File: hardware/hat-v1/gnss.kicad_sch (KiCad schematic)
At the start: 10 parts, among them J4 U.FL, U14 MAX-M10S-00B

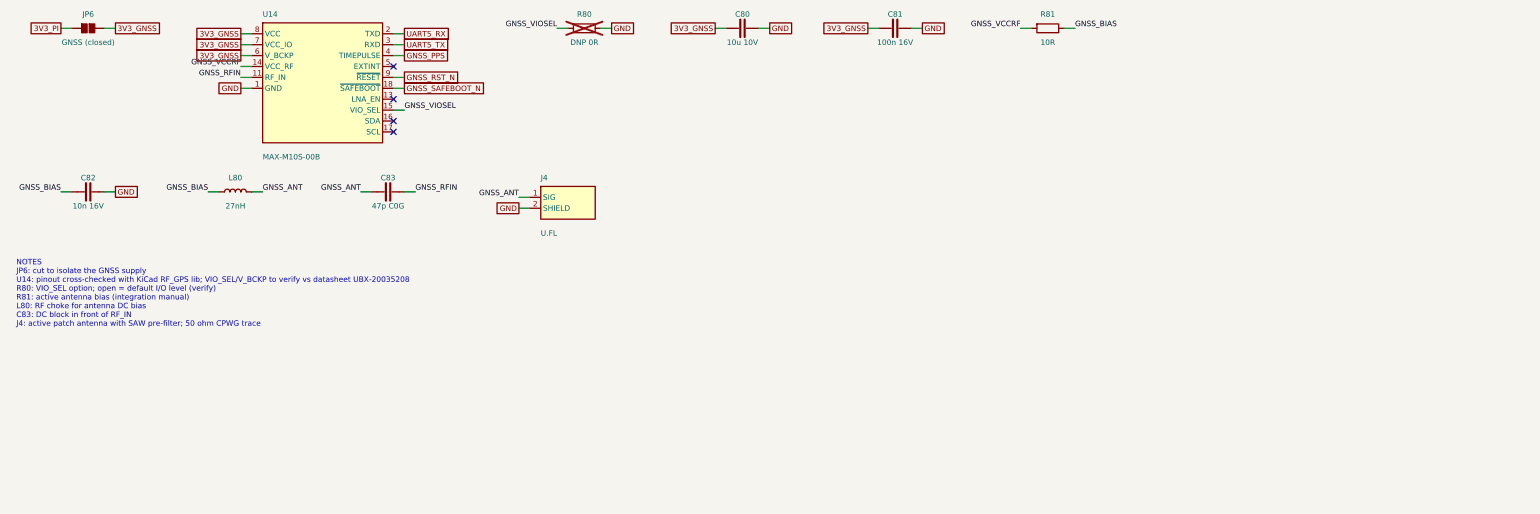
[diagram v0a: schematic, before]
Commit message: HAT v1 schematic: apply adversarial review (power + digital/security/DFM)
AUTO-ON above buck EN window, BENCH no longer blocks power-off, OVP moved
to 19.2 V with input damper, Tier A parts DNP for JLC, debug links
removable for production, antenna short limited, stock footprints where
available, cap ratings/DC-bias fixes, CONSOLE_TX/RX naming.

Co-Authored-By: Claude Opus 5.5 <noreply@anthropic.com>
Claude-Session: https://claude.ai/code/session_01MLRuxTEmuMV82xcNLE62jW
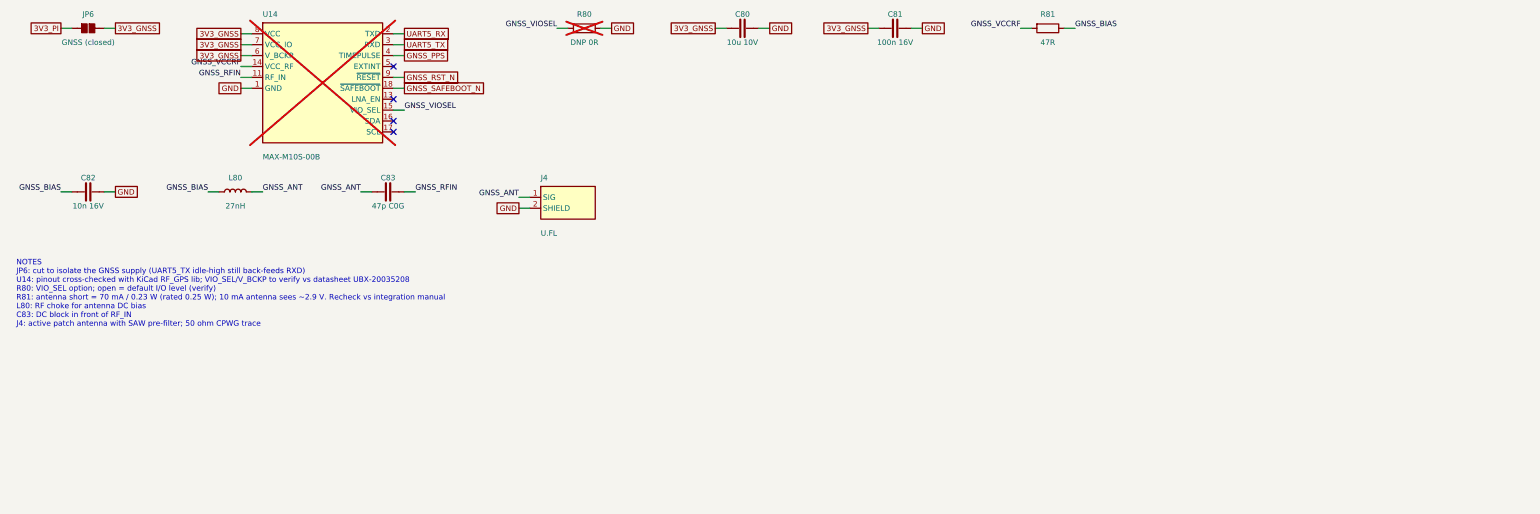
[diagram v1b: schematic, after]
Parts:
- JP6: Note cut to isolate the GNSS supply -> cut to isolate the GNSS supply (UART5_TX idle-high still ba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; now left out of the parts list
- R81: value 10R -> 47R; footprint Resistor_SMD:R_0402_1005Metric -> Resistor_SMD:R_1206_3216Metric; Note active antenna bias (integration manual) -> antenna short = 70 mA / 0.23 W (rated 0.25 W); 10 mA antenn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
- U14: now not fitted
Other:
- note added: "NOTES JP6: cut to isolate the GNSS supply (UART5_TX idle-high still back-feeds RXD) U14: pinout cross-checked with KiCad RF_GPS lib; VIO_SEL/V_BCKP to verify vs datasheet UBX-20035208 R80: VIO_SEL option; open = default I/O level (verify) R81: antenna short = 70 mA / 0.23 W (rated 0.25 W); 10 mA antenna sees ~2.9 V. Recheck vs integration manual L80: RF choke for antenna DC bias C83: DC block in 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"
- note removed: "NOTES JP6: cut to isolate the GNSS supply U14: pinout cross-checked with KiCad RF_GPS lib; VIO_SEL/V_BCKP to verify vs datasheet UBX-20035208 R80: VIO_SEL option; open = default I/O level (verify) R81: active antenna bias (integration manual) L80: RF choke for antenna DC bias C83: DC block in front of RF_IN J4: active patch antenna with SAW pre-filter; 50 ohm CPWG trace"
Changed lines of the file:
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@@
   (paper "A4")
   (title_block (title "Batman HAT v1 (Pi 4) - replaces Seeed WM1302 HAT") (date "2026-09-27") (rev "0.1-draft") (company "Batman project - generated by hardware/hat-v1/gen/gen_sch.py, do not edit by hand") (comment 1 "8 GNSS MAX-M10S + active antenna bias") (comment 2 "Label-based schematic: same net name = connected"))
-  (symbol (lib_id "batman:SJ") (at 31.75 26.67 0) (unit 1) (in_bom yes) (on_board yes) (dnp no)
+  (symbol (lib_id "batman:SJ") (at 31.75 26.67 0) (unit 1) (in_bom no) (on_board yes) (dnp no)
     (property "Reference" "JP6" (at 31.75 24.13 0) (effects (font (size 1.27 1.27)) (justify bottom)))
     (property "Value" "GNSS (closed)" (at 31.75 29.21 0) (effects (font (size 1.27 1.27)) (justify top)))
@@
     (property "Tier" "C" (at 31.75 26.67 0) (effects (font (size 1.27 1.27)) hide))
     (property "LCSC" "" (at 31.75 26.67 0) (effects (font (size 1.27 1.27)) hide))
-    (property "Note" "cut to isolate the GNSS supply" (at 31.75 26.67 0) (effects (font (size 1.27 1.27)) hide))
+    (property "Note" "cut to isolate the GNSS supply (UART5_TX idle-high still back-feeds RXD)" (at 31.75 26.67 0) (effects (font (size 1.27 1.27)) hide))
     (pin "1")
     (pin "2")
@@
   (global_label "3V3_GNSS" (shape passive) (at 38.1 26.67 0) (fields_autoplaced) (effects (font (size 1.27 1.27)) (justify left))
     (property "Intersheetrefs" "${INTERSHEET_REFS}" (at 38.1 26.67 0) (effects (font (size 1.27 1.27)) hide)))
-  (symbol (lib_id "batman:MAXM10S") (at 86.36 39.37 0) (unit 1) (in_bom yes) (on_board yes) (dnp no)
+  (symbol (lib_id "batman:MAXM10S") (at 86.36 39.37 0) (unit 1) (in_bom yes) (on_board yes) (dnp yes)
     (property "Reference" "U14" (at 72.39 24.13 0) (effects (font (size 1.27 1.27)) (justify left bottom)))
     (property "Value" "MAX-M10S-00B" (at 72.39 55.88 0) (effects (font (size 1.27 1.27)) (justify left top)))
@@
   (symbol (lib_id "batman:R") (at 255.27 26.67 0) (unit 1) (in_bom yes) (on_board yes) (dnp no)
     (property "Reference" "R81" (at 255.27 24.13 0) (effects (font (size 1.27 1.27)) (justify bottom)))
-    (property "Value" "10R" (at 255.27 29.21 0) (effects (font (size 1.27 1.27)) (justify top)))
-    (property "Footprint" "Resistor_SMD:R_0402_1005Metric" (at 255.27 26.67 0) (effects (font (size 1.27 1.27)) hide))
+    (property "Value" "47R" (at 255.27 29.21 0) (effects (font (size 1.27 1.27)) (justify top)))
+    (property "Footprint" "Resistor_SMD:R_1206_3216Metric" (at 255.27 26.67 0) (effects (font (size 1.27 1.27)) hide))
     (property "Datasheet" "" (at 255.27 26.67 0) (effects (font (size 1.27 1.27)) hide))
     (property "MPN" "" (at 255.27 26.67 0) (effects (font (size 1.27 1.27)) hide))
@@
     (property "Tier" "C" (at 255.27 26.67 0) (effects (font (size 1.27 1.27)) hide))
     (property "LCSC" "" (at 255.27 26.67 0) (effects (font (size 1.27 1.27)) hide))
-    (property "Note" "active antenna bias (integration manual)" (at 255.27 26.67 0) (effects (font (size 1.27 1.27)) hide))
+    (property "Note" "antenna short = 70 mA / 0.23 W (rated 0.25 W); 10 mA antenna sees ~2.9 V. Recheck vs integration manual" (at 255.27 26.67 0) (effects (font (size 1.27 1.27)) hide))
     (pin "1")
     (pin "2")
@@
   (global_label "GND" (shape passive) (at 132.08 68.58 180) (fields_autoplaced) (effects (font (size 1.27 1.27)) (justify right))
     (property "Intersheetrefs" "${INTERSHEET_REFS}" (at 132.08 68.58 0) (effects (font (size 1.27 1.27)) hide)))
-  (text "NOTES\nJP6: cut to isolate the GNSS supply\nU14: pinout cross-checked with KiCad RF_GPS lib; VIO_SEL/V_BCKP to verify vs datasheet UBX-20035208\nR80: VIO_SEL option; open = default I/O level (verify)\nR81: active antenna bias (integration manual)\nL80: RF choke for antenna DC bias\nC83: DC block in front of RF_IN\nJ4: active patch antenna with SAW pre-filter; 50 ohm CPWG trace" (at 15 80.56 0) (effects (font (size 1.27 1.27)) (justify left top)))
+  (text "NOTES\nJP6: cut to isolate the GNSS supply (UART5_TX idle-high still back-feeds RXD)\nU14: pinout cross-checked with KiCad RF_GPS lib; VIO_SEL/V_BCKP to verify vs datasheet UBX-20035208\nR80: VIO_SEL option; open = default I/O level (verify)\nR81: antenna short = 70 mA / 0.23 W (rated 0.25 W); 10 mA antenna sees ~2.9 V. Recheck vs integration manual\nL80: RF choke for antenna DC bias\nC83: DC block in front of RF_IN\nJ4: active patch antenna with SAW pre-filter; 50 ohm CPWG trace" (at 15 80.56 0) (effects (font (size 1.27 1.27)) (justify left top)))
 )

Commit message: HAT v1: GNSS per MAX-M10S datasheet R08 (VIO_SEL open, VCC_RF 50 mA -> R81 68R)
Co-Authored-By: Claude Opus 5.5 <noreply@anthropic.com>
Claude-Session: https://claude.ai/code/session_01MLRuxTEmuMV82xcNLE62jW
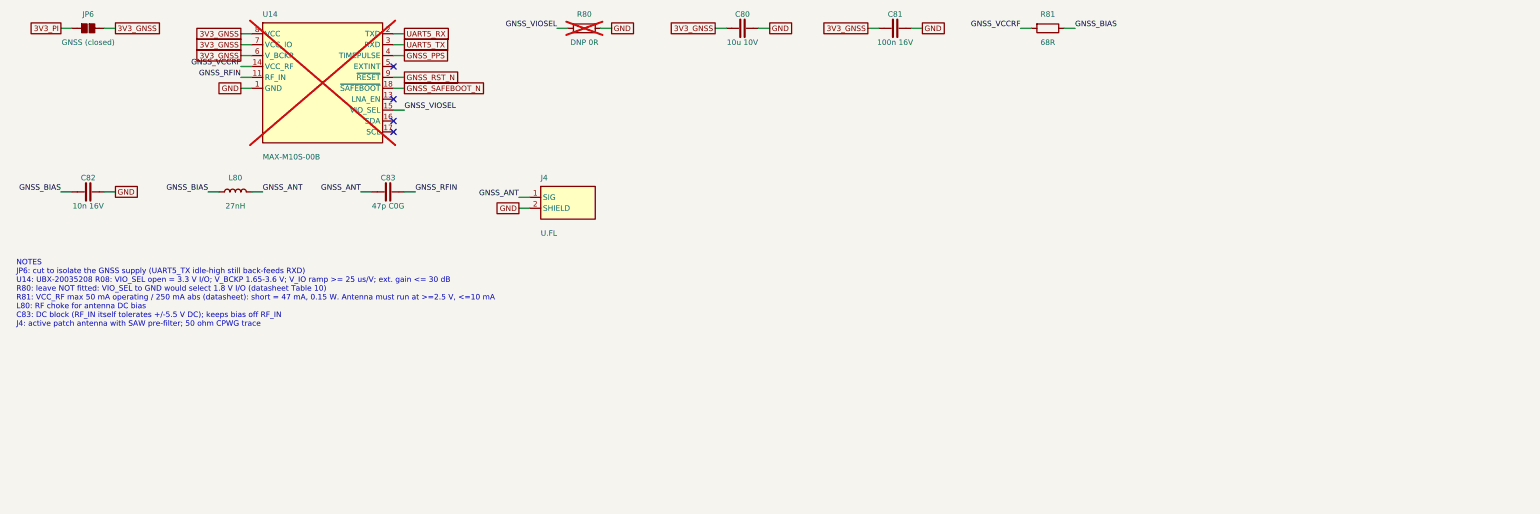
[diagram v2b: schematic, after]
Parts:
- C83: Note DC block in front of RF_IN -> DC block (RF_IN itself tolerates +/-5.5 V DC); keeps bias o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
- R80: Note VIO_SEL option; open = default I/O level (verify) -> leave NOT fitted: VIO_SEL to GND would select 1.8 V I/O (da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
- R81: value 47R -> 68R; Note antenna short = 70 mA / 0.23 W (rated 0.25 W); 10 mA antenn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 -> VCC_RF max 50 mA operating / 250 mA abs (datasheet): short 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
- U14: Note pinout cross-checked with KiCad RF_GPS lib; VIO_SEL/V_BCKP 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 -> UBX-20035208 R08: VIO_SEL open = 3.3 V I/O; V_BCKP 1.65-3.6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
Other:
- note added: "NOTES JP6: cut to isolate the GNSS supply (UART5_TX idle-high still back-feeds RXD) U14: UBX-20035208 R08: VIO_SEL open = 3.3 V I/O; V_BCKP 1.65-3.6 V; V_IO ramp >= 25 us/V; ext. gain <= 30 dB R80: leave NOT fitted: VIO_SEL to GND would select 1.8 V I/O (datasheet Table 10) R81: VCC_RF max 50 mA operating / 250 mA abs (datasheet): short = 47 mA, 0.15 W. Antenna must run at >=2.5 V, <=10 mA L80: R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"
- note removed: "NOTES JP6: cut to isolate the GNSS supply (UART5_TX idle-high still back-feeds RXD) U14: pinout cross-checked with KiCad RF_GPS lib; VIO_SEL/V_BCKP to verify vs datasheet UBX-20035208 R80: VIO_SEL option; open = default I/O level (verify) R81: antenna short = 70 mA / 0.23 W (rated 0.25 W); 10 mA antenna sees ~2.9 V. Recheck vs integration manual L80: RF choke for antenna DC bias C83: DC block in 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"
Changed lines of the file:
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@@
     (property "Tier" "A" (at 86.36 39.37 0) (effects (font (size 1.27 1.27)) hide))
     (property "LCSC" "" (at 86.36 39.37 0) (effects (font (size 1.27 1.27)) hide))
-    (property "Note" "pinout cross-checked with KiCad RF_GPS lib; VIO_SEL/V_BCKP to verify vs datasheet UBX-20035208" (at 86.36 39.37 0) (effects (font (size 1.27 1.27)) hide))
+    (property "Note" "UBX-20035208 R08: VIO_SEL open = 3.3 V I/O; V_BCKP 1.65-3.6 V; V_IO ramp >= 25 us/V; ext. gain <= 30 dB" (at 86.36 39.37 0) (effects (font (size 1.27 1.27)) hide))
     (pin "8")
     (pin "7")
@@
     (property "Tier" "C" (at 147.32 26.67 0) (effects (font (size 1.27 1.27)) hide))
     (property "LCSC" "" (at 147.32 26.67 0) (effects (font (size 1.27 1.27)) hide))
-    (property "Note" "VIO_SEL option; open = default I/O level (verify)" (at 147.32 26.67 0) (effects (font (size 1.27 1.27)) hide))
+    (property "Note" "leave NOT fitted: VIO_SEL to GND would select 1.8 V I/O (datasheet Table 10)" (at 147.32 26.67 0) (effects (font (size 1.27 1.27)) hide))
     (pin "1")
     (pin "2")
@@
   (symbol (lib_id "batman:R") (at 255.27 26.67 0) (unit 1) (in_bom yes) (on_board yes) (dnp no)
     (property "Reference" "R81" (at 255.27 24.13 0) (effects (font (size 1.27 1.27)) (justify bottom)))
-    (property "Value" "47R" (at 255.27 29.21 0) (effects (font (size 1.27 1.27)) (justify top)))
+    (property "Value" "68R" (at 255.27 29.21 0) (effects (font (size 1.27 1.27)) (justify top)))
     (property "Footprint" "Resistor_SMD:R_1206_3216Metric" (at 255.27 26.67 0) (effects (font (size 1.27 1.27)) hide))
     (property "Datasheet" "" (at 255.27 26.67 0) (effects (font (size 1.27 1.27)) hide))
@@
     (property "Tier" "C" (at 255.27 26.67 0) (effects (font (size 1.27 1.27)) hide))
     (property "LCSC" "" (at 255.27 26.67 0) (effects (font (size 1.27 1.27)) hide))
-    (property "Note" "antenna short = 70 mA / 0.23 W (rated 0.25 W); 10 mA antenna sees ~2.9 V. Recheck vs integration manual" (at 255.27 26.67 0) (effects (font (size 1.27 1.27)) hide))
+    (property "Note" "VCC_RF max 50 mA operating / 250 mA abs (datasheet): short = 47 mA, 0.15 W. Antenna must run at >=2.5 V, <=10 mA" (at 255.27 26.67 0) (effects (font (size 1.27 1.27)) hide))
     (pin "1")
     (pin "2")
@@
     (property "Tier" "C" (at 101.6 64.77 0) (effects (font (size 1.27 1.27)) hide))
     (property "LCSC" "" (at 101.6 64.77 0) (effects (font (size 1.27 1.27)) hide))
-    (property "Note" "DC block in front of RF_IN" (at 101.6 64.77 0) (effects (font (size 1.27 1.27)) hide))
+    (property "Note" "DC block (RF_IN itself tolerates +/-5.5 V DC); keeps bias off RF_IN" (at 101.6 64.77 0) (effects (font (size 1.27 1.27)) hide))
     (pin "1")
     (pin "2")
@@
   (global_label "GND" (shape passive) (at 132.08 68.58 180) (fields_autoplaced) (effects (font (size 1.27 1.27)) (justify right))
     (property "Intersheetrefs" "${INTERSHEET_REFS}" (at 132.08 68.58 0) (effects (font (size 1.27 1.27)) hide)))
-  (text "NOTES\nJP6: cut to isolate the GNSS supply (UART5_TX idle-high still back-feeds RXD)\nU14: pinout cross-checked with KiCad RF_GPS lib; VIO_SEL/V_BCKP to verify vs datasheet UBX-20035208\nR80: VIO_SEL option; open = default I/O level (verify)\nR81: antenna short = 70 mA / 0.23 W (rated 0.25 W); 10 mA antenna sees ~2.9 V. Recheck vs integration manual\nL80: RF choke for antenna DC bias\nC83: DC block in front of RF_IN\nJ4: active patch antenna with SAW pre-filter; 50 ohm CPWG trace" (at 15 80.56 0) (effects (font (size 1.27 1.27)) (justify left top)))
+  (text "NOTES\nJP6: cut to isolate the GNSS supply (UART5_TX idle-high still back-feeds RXD)\nU14: UBX-20035208 R08: VIO_SEL open = 3.3 V I/O; V_BCKP 1.65-3.6 V; V_IO ramp >= 25 us/V; ext. gain <= 30 dB\nR80: leave NOT fitted: VIO_SEL to GND would select 1.8 V I/O (datasheet Table 10)\nR81: VCC_RF max 50 mA operating / 250 mA abs (datasheet): short = 47 mA, 0.15 W. Antenna must run at >=2.5 V, <=10 mA\nL80: RF choke for antenna DC bias\nC83: DC block (RF_IN itself tolerates +/-5.5 V DC); keeps bias off RF_IN\nJ4: active patch antenna with SAW pre-filter; 50 ohm CPWG trace" (at 15 80.56 0) (effects (font (size 1.27 1.27)) (justify left top)))
 )

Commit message: HAT v1: GNSS 3-pin antenna supervisor (UBX-20053088 Fig 38) + RTC coin-cell backup
Antenna supply switched by LNA_EN, 10R sense, OPA333 comparator for open
detection, SCL/SDA reused for ANT_SHORT_N/ANT_DETECT. RTC backup moves to
a Seiko MS rechargeable cell with 1k series resistor (App Manual 7.3);
overlay trickle 15k. Cell footprint does not fit yet (floorplan).

Co-Authored-By: Claude Opus 5.5 <noreply@anthropic.com>
Claude-Session: https://claude.ai/code/session_01MLRuxTEmuMV82xcNLE62jW
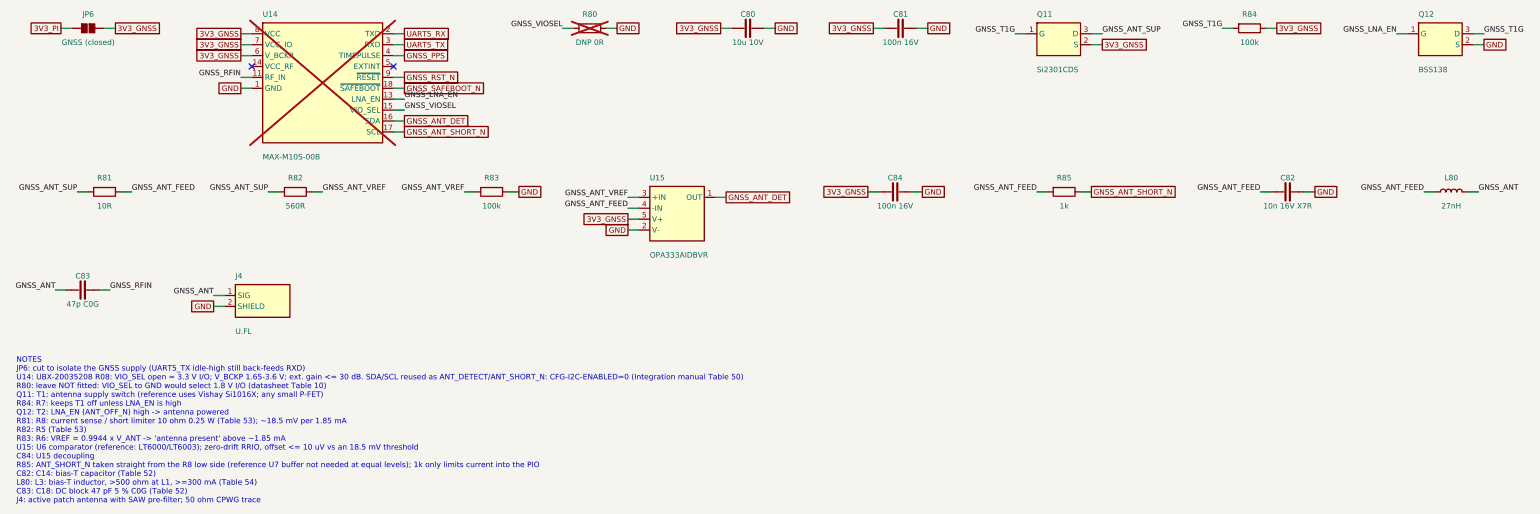
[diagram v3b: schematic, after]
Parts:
- added C84: 100n 16V, Capacitor_SMD:C_0402_1005Metric, symbol batman:C
- added Q11: Si2301CDS, Package_TO_SOT_SMD:SOT-23, symbol batman:PMOS
- added Q12: BSS138, Package_TO_SOT_SMD:SOT-23, symbol batman:NMOS
- added R82: 560R, Resistor_SMD:R_0402_1005Metric, symbol batman:R
- added R83, R84: 100k, Resistor_SMD:R_0402_1005Metric, symbol batman:R
- added R85: 1k, Resistor_SMD:R_0402_1005Metric, symbol batman:R
- added U15: OPA333AIDBVR, Package_TO_SOT_SMD:SOT-23-5, symbol batman:OPAMP5
- C82: value 10n 16V -> 10n 16V X7R; Note (none) -> C14: bias-T capacitor (Table 52)
- C83: Note DC block (RF_IN itself tolerates +/-5.5 V DC); keeps bias o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 -> C18: DC block 47 pF 5 % C0G (Table 52)
- L80: Note RF choke for antenna DC bias -> L3: bias-T inductor, >500 ohm at L1, >=300 mA (Table 54)
- R81: value 68R -> 10R; Note VCC_RF max 50 mA operating / 250 mA abs (datasheet): short 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 -> R8: current sense / short limiter 10 ohm 0.25 W (Table 53);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
- U14: Note UBX-20035208 R08: VIO_SEL open = 3.3 V I/O; V_BCKP 1.65-3.6 V; V_IO ramp >= 25 us/V; ext. gain <= 30 dB -> UBX-20035208 R08: VIO_SEL open = 3.3 V I/O; V_BCKP 1.65-3.6 V; ext. gain <= 30 dB. SDA/SCL reused as ANT_DETECT/ANT_SHORT_N: CFG-I2C-ENABLED=0 (Integration manual Table 50)
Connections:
- net 3V3_GNSS: now also C84.1, Q11.2 (S), R84.2, U15.5 (V+)
- net GND: now also C84.2, Q12.2 (S), R83.2, U15.2 (V-)
- net GNSS_LNA_EN: now reaches U14.13 (LNA_EN)
- net GNSS_LNA_EN: now also Q12.1 (G)
- net GNSS_ANT_DET: now reaches U14.16 (SDA)
- net GNSS_ANT_DET: now also U15.1 (OUT)
- net GNSS_ANT_SHORT_N: now reaches U14.17 (SCL)
- net GNSS_ANT_SHORT_N: now also R85.2
- net GNSS_BIAS renamed GNSS_ANT_FEED
- net GNSS_ANT_FEED: now also R85.1, U15.4 (-IN)
- net GNSS_VCCRF: no longer names the net of U14.14 (VCC_RF)
- net GNSS_VCCRF: no longer R81.1
- new net GNSS_ANT_SUP: Q11.3 (D), R81.1, R82.1
- new net GNSS_ANT_VREF: R82.2, R83.1, U15.3 (+IN)
- new net GNSS_T1G: Q11.1 (G), Q12.3 (D), R84.1
- no-connect marks 4 -> 2
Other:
- note added: "NOTES JP6: cut to isolate the GNSS supply (UART5_TX idle-high still back-feeds RXD) U14: UBX-20035208 R08: VIO_SEL open = 3.3 V I/O; V_BCKP 1.65-3.6 V; ext. gain <= 30 dB. SDA/SCL reused as ANT_DETECT/ANT_SHORT_N: CFG-I2C-ENABLED=0 (Integration manual Table 50) R80: leave NOT fitted: VIO_SEL to GND would select 1.8 V I/O (datasheet Table 10) Q11: T1: antenna supply switch (reference uses Vishay S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"
- note removed: "NOTES JP6: cut to isolate the GNSS supply (UART5_TX idle-high still back-feeds RXD) U14: UBX-20035208 R08: VIO_SEL open = 3.3 V I/O; V_BCKP 1.65-3.6 V; V_IO ramp >= 25 us/V; ext. gain <= 30 dB R80: leave NOT fitted: VIO_SEL to GND would select 1.8 V I/O (datasheet Table 10) R81: VCC_RF max 50 mA operating / 250 mA abs (datasheet): short = 47 mA, 0.15 W. Antenna must run at >=2.5 V, <=10 mA L80: R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"
- moved on the sheet: C80, C81, C82, C83, J4, L80, R80, R81
